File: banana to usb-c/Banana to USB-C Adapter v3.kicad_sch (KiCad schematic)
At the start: 12 parts, among them J1 USB4125-GF-A-0190, J2 Positive, J3 Negative

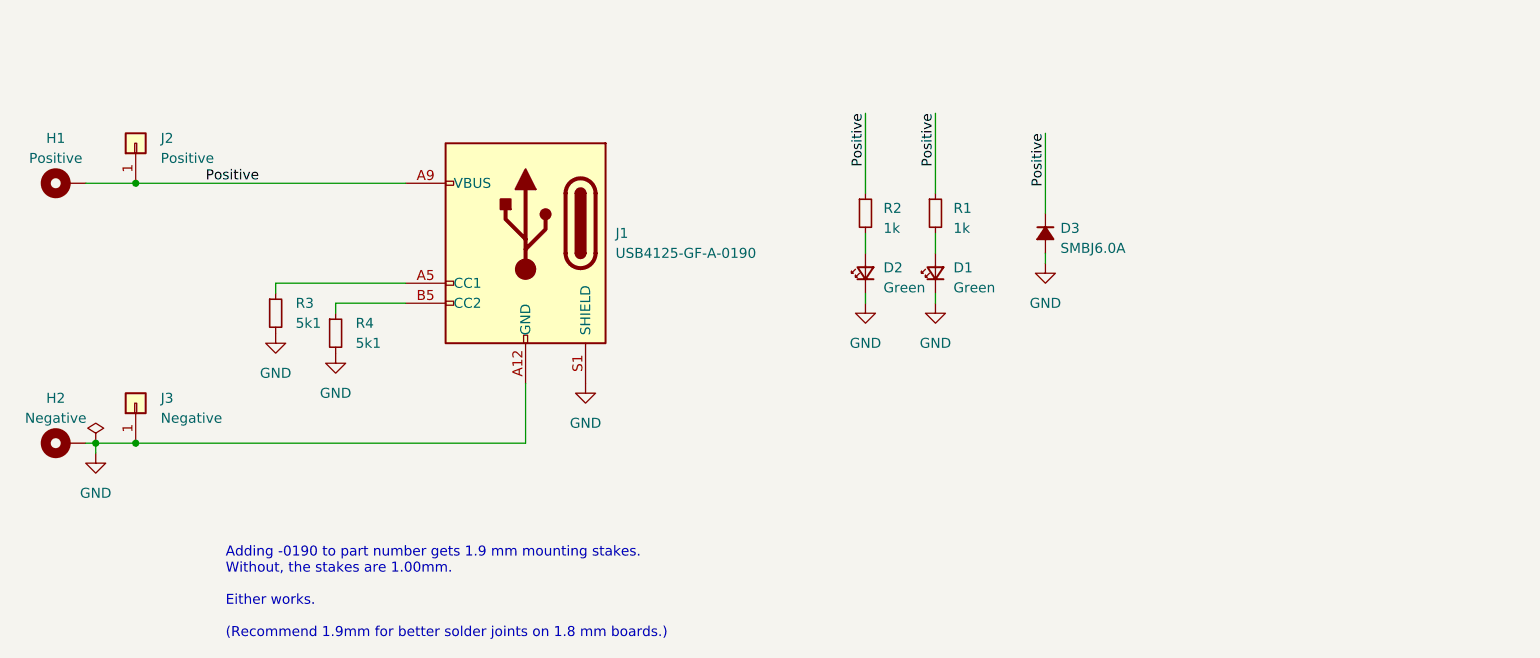
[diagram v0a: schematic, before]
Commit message: sch: changed resistors to pull-up and added link to kb article
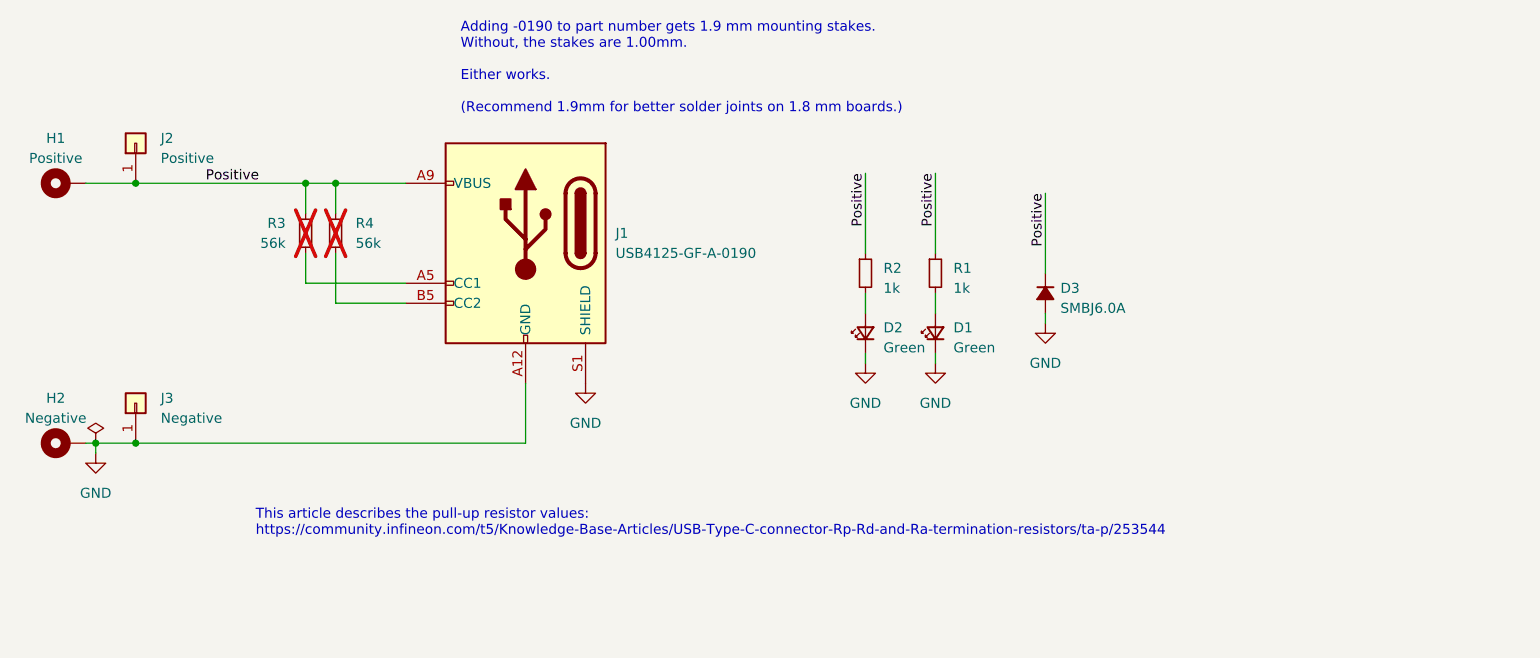
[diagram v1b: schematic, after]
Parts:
- R3, R4: value 5k1 -> 56k; now not fitted
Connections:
- net GND: no longer R3.2, R4.2
- net Positive: now also R3.1, R4.1
- net at J1.A5 (CC1): now also R3.2; no longer R3.1
- net at J1.B5 (CC2): now also R4.2; no longer R4.1
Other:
- note added: "This article describes the pull-up resistor values: https://community.infineon.com/t5/Knowledge-Base-Articles/USB-Type-C-connector-Rp-Rd-and-Ra-termination-resistors/ta-p/253544"
- moved on the sheet: D1, D2, D3, R1, R2
